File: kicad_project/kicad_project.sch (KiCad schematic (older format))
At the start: 157 parts, among them U1 SST39SF010, U11 AS6C4008-55PCN, U12 74LS85, U13 74LS85, U14 74LS283, U15 AS6C4008-55PCN, U16 74HC245, U17 74HC245, U18 74LS283, U19 74HC86, U2 SST39SF010, U20 74HC245, U21 74HC245, U22 74HC245, U23 SST39SF010, U24 74HC86, U25 74LS283, U26 74HC245, U27 74HC245, U28 74HC245, U29 74HC86, U3 74HC245, U30 74LS283, U31 SST39SF010, U4 74HC245, U5 74LS161, U6 74HC245, U7 74HC245, U8 74HC245, U9 SST39SF010

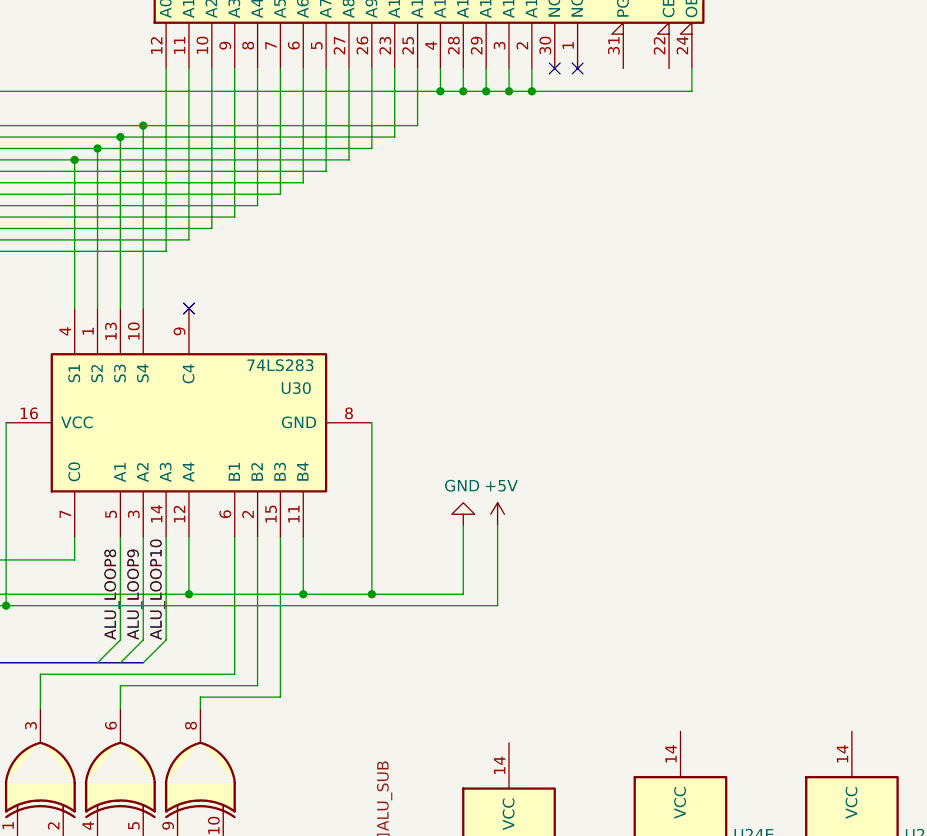
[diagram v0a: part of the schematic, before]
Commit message: Added some flashing tools, and misc...
Signed-off-by: Dave Butler <croepha@gmail.com>
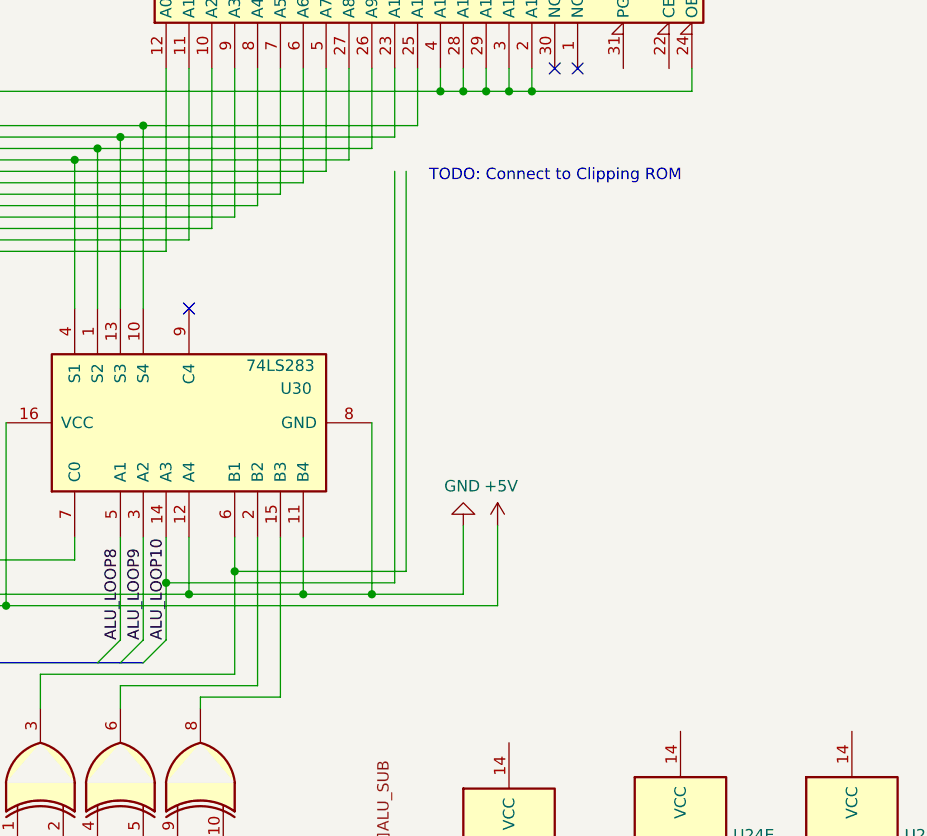
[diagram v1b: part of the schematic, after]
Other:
- note added: "TODO: Connect to Clipping ROM"

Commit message: .
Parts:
- added R?: 10K, symbol Device:R
- added U? (x6): 74HC595, symbol 74xx:74HC595
- added U? (x2): 74AHC04, symbol 74xx:74AHC04
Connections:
- net labels added: PRGM#, PRGMCLK, PRGMIN, PRGMOUT
- wire segments 1643 -> 1888
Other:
- moved on the sheet: R1, R2, R3, R4, U11, U12, U13, U14, U15, U16, U17, U5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

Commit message: .
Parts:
- renumbered U9 to CONTROL2
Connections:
- net labels added: BUS_SIGN, PC_LDBUS#, PC_LDEND#, PC_LDSUM#, PC_SUM_SIGN
- net labels removed: PC_LD, PC_LDBUS, PC_LDEND, PC_LDSUM, PC_RNEG, PC_ROVR
- wire segments 1888 -> 1892
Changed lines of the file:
@@
 Connection ~ 4700 14750
 Wire Wire Line
-	5400 14750 7100 14750
+	5400 14750 6150 14750
 Connection ~ 5000 14750
 Wire Wire Line
 	5100 14750 5000 14750
 Wire Wire Line
-	4000 14750 4300 14750
+	4000 14750 4250 14750
 Wire Wire Line
 	4600 14750 4700 14750
@@
 	21100 8250 21100 8000
 Wire Wire Line
-	21100 8250 18150 8250
-Wire Wire Line
 	21000 8350 18150 8350
 Wire Wire Line
@@
 Wire Wire Line
 	16200 13850 16200 16500
-Wire Wire Line
-	16150 14050 16150 16400
 $Comp
 L Memory_RAM:AS6C4008-55PCN U15
@@
 	16200 16500 15700 16500
 Text HLabel 15700 16500 0    50   Output ~ 0
-PC_RNEG
-Text HLabel 15700 16400 0    50   Output ~ 0
-PC_ROVR
+PC_SUM_SIGN
+Text HLabel 17700 8250 0    50   Output ~ 0
+BUS_SIGN
 Wire Wire Line
 	17350 14350 17250 14350
@@
 PC_CEQE
 Text HLabel 14850 17050 2    50   Input ~ 0
-PC_LDEND
+PC_LDEND#
 Text HLabel 14850 16850 2    50   Input ~ 0
-PC_LDBUS
+PC_LDBUS#
 Text HLabel 14850 16950 2    50   Input ~ 0
-PC_LDSUM
+PC_LDSUM#
 Wire Wire Line
 	14850 16650 14750 16650
@@
 	25900 6200 25900 8400
 Wire Wire Line
-	15700 16400 16150 16400
-Wire Wire Line
 	19100 19000 19100 19750
 Wire Wire Line
@@
 Wire Wire Line
 	28150 3900 28150 3550
-Text HLabel 17250 3150 2    50   Output ~ 0
+Text HLabel 17250 3300 2    50   Output ~ 0
 WRITE_READY
-Text HLabel 15500 3300 3    50   Input ~ 0
+Text HLabel 15500 3950 3    50   Input ~ 0
 READY_DOWN
-Text HLabel 15400 3300 3    50   Input ~ 0
+Text HLabel 15400 3950 3    50   Input ~ 0
 READY_UP
-Text HLabel 15300 3300 3    50   Input ~ 0
+Text HLabel 15300 3950 3    50   Input ~ 0
 READY_RIGHT
-Text HLabel 15200 3300 3    50   Input ~ 0
+Text HLabel 15200 3950 3    50   Input ~ 0
 READY_LEFT
-Text HLabel 11250 3300 3    50   Input ~ 0
-ACC_NEG
-Text HLabel 11150 3300 3    50   Input ~ 0
-ACC_EQZ
-Text HLabel 11050 3300 3    50   Input ~ 0
-PC_ROVR
-Text HLabel 10950 3300 3    50   Input ~ 0
-PC_ROVR
-Text HLabel 10850 3300 3    50   Input ~ 0
-PC_ROVR
-Text HLabel 10750 3300 3    50   Input ~ 0
-PC_ROVR
 Wire Wire Line
 	18700 6700 18700 2850
@@
 NoConn ~ 17250 2750
 Wire Wire Line
-	20200 3050 20200 2850
+	20200 3200 20200 2850
 Wire Wire Line
 	20100 2950 20100 2850
 Wire Wire Line
-	20000 2850 20000 2950
-Connection ~ 20000 2950
-Wire Wire Line
-	20000 2950 20100 2950
-Wire Wire Line
-	19900 2850 19900 2950
-Connection ~ 19900 2950
-Wire Wire Line
-	19900 2950 20000 2950
-Wire Wire Line
-	19800 2850 19800 2950
-Connection ~ 19800 2950
-Wire Wire Line
-	19800 2950 19900 2950
-Wire Wire Line
-	19700 2850 19700 2950
-Connection ~ 19700 2950
-Wire Wire Line
-	19700 2950 19800 2950
-Wire Wire Line
-	19500 2950 19500 2850
-Connection ~ 19500 2950
-Wire Wire Line
-	19500 2950 19600 2950
-Wire Wire Line
-	19400 2850 19400 2950
-Connection ~ 19400 2950
-Wire Wire Line
-	19400 2950 19500 2950
-Wire Wire Line
-	19600 2850 19600 2950
-Connection ~ 19600 2950
-Wire Wire Line
-	19600 2950 19700 2950
-Wire Wire Line
 	9750 2850 9750 6700
 Wire Wire Line
-	16950 3050 20200 3050
+	16950 3200 20200 3200
 Connection ~ 15600 2950
 Wire Wire Line
@@
 Wire Wire Line
 	13900 2950 15600 2950
-Connection ~ 16950 3050
+Connection ~ 16950 3200
 Connection ~ 12500 3100
 Wire Wire Line
@@
 	12500 3100 15000 3100
 Wire Wire Line
-	15500 3300 15500 2850
+	15500 3950 15500 2850
 Wire Wire Line
-	15400 2850 15400 3300
+	15400 2850 15400 3950
 Wire Wire Line
-	15300 3300 15300 2850
+	15300 3950 15300 2850
 Wire Wire Line
-	15200 2850 15200 3300
+	15200 2850 15200 3950
 Wire Wire Line
-	15700 3050 16950 3050
+	15700 3200 16950 3200
 Wire Wire Line
-	15700 2850 15700 3050
+	15700 2850 15700 3200
 Wire Wire Line
-	16950 3050 16950 2750
+	16950 3200 16950 2750
 NoConn ~ 12700 2750
 Wire Wire Line
-	11250 2850 11250 3300
-Wire Wire Line
-	11150 3300 11150 2850
-Wire Wire Line
-	11050 2850 11050 3300
-Wire Wire Line
-	10950 3300 10950 2850
-Wire Wire Line
-	10850 2850 10850 3300
-Wire Wire Line
-	10750 3300 10750 2850
-Wire Wire Line
 	15100 3150 15100 2850
 Wire Wire Line
@@
 Wire Wire Line
 	9650 6750 9650 2850
-Connection ~ 18450 2950
 Wire Wire Line
 	15600 2950 18450 2950
 Wire Wire Line
-	18450 2950 19400 2950
-Wire Wire Line
 	18600 6750 18600 2850
 $Comp
@@
 	0    -1   1    0
 $EndComp
-Text HLabel 9650 1050 1    50   Output ~ 0
-PC_LD
-Text HLabel 9750 1050 1    50   Output ~ 0
-PC_LDEND
-Text HLabel 9850 1050 1    50   Output ~ 0
-PC_LDBUS
-Text HLabel 9950 1050 1    50   Output ~ 0
-PC_LDSUM
+Text HLabel 19000 1050 1    50   Output ~ 0
+PC_LD#
+Text HLabel 19100 1050 1    50   Output ~ 0
+PC_LDEND#
+Text HLabel 19200 1050 1    50   Output ~ 0
+PC_LDBUS#
+Text HLabel 19300 1050 1    50   Output ~ 0
+PC_LDSUM#
 Wire Wire Line
-	9650 1050 9650 1650
+	19000 1050 19000 1650
 Wire Wire Line
-	9750 1650 9750 1050
+	19100 1650 19100 1050
 Wire Wire Line
-	9850 1050 9850 1650
+	19200 1050 19200 1650
 Wire Wire Line
-	9950 1050 9950 1650
+	19300 1050 19300 1650
 Text HLabel 10050 1050 1    50   Output ~ 0
 G_LEFT
@@
 H1
 Text HLabel 14300 1050 1    50   Output ~ 0
-H1
+H2
 NoConn ~ 12700 1750
 Wire Wire Line
@@
 Connection ~ 17950 1450
 Wire Wire Line
-	19100 1050 19100 1650
-Text HLabel 19100 1050 1    50   Output ~ 0
+	9750 1050 9750 1650
+Text HLabel 9750 1050 1    50   Output ~ 0
 ALU_RDACC#
 Wire Wire Line
@@
 	18600 1050 18600 1650
 Wire Wire Line
-	19300 1650 19300 1050
+	9950 1650 9950 1050
 Wire Wire Line
-	19200 1050 19200 1650
-Text HLabel 19300 1050 1    50   Output ~ 0
+	9850 1050 9850 1650
+Text HLabel 9950 1050 1    50   Output ~ 0
 BAK_RESTORE#
-Text HLabel 19200 1050 1    50   Output ~ 0
+Text HLabel 9850 1050 1    50   Output ~ 0
 BAK_SAVE#
 Wire Wire Line
-	19000 1050 19000 1650
-Text HLabel 19000 1050 1    50   Output ~ 0
+	9650 1050 9650 1650
+Text HLabel 9650 1050 1    50   Output ~ 0
 ALU_WRACC#
 Text HLabel 18800 1050 1    50   Output ~ 0
@@
 NoConn ~ 17050 1750
 $Comp
-L Memory_Flash:SST39SF010 U9
+L Memory_Flash:SST39SF010 CONTROL2
 U 1 1 9D597AA5
 P 19800 2250
-F 0 "U9" V 20100 2050 50  0000 C CNN
+F 0 "CONTROL2" V 20100 1350 50  0000 C CNN
 F 1 "SST39SF010" V 20100 2400 50  0000 C CNN
 F 2 "" H 19800 2550 50  0001 C CNN
@@
 	16100 8100 16750 8100
 Wire Wire Line
-	16950 3050 16950 3150
+	16950 3200 16950 3300
 Wire Wire Line
-	16950 3150 17250 3150
+	16950 3300 17250 3300
 Connection ~ 16150 8150
 Wire Wire Line
@@
 TODO: Connect to Clipping ROM
 Wire Wire Line
-	5600 5000 6900 5000
-Wire Bus Line
-	6800 3650 6800 6000
-Wire Wire Line
 	16100 6900 16100 7500
 Connection ~ 16100 7500
@@
 Connection ~ 16950 6050
 Connection ~ 17050 6000
-Wire Wire Line
-	11950 3000 9550 3000
 Connection ~ 11950 3000
 Wire Wire Line
@@
 Wire Wire Line
 	12200 8800 12200 8600
-Wire Wire Line
-	11700 8800 11800 8800
 Connection ~ 11700 8800
 Wire Wire Line
@@
 Wire Wire Line
 	12200 8900 11800 8900
-Wire Wire Line
-	11800 8900 11800 8800
-Connection ~ 11800 8800
-Wire Wire Line
-	11800 8800 11900 8800
 Connection ~ 12200 8600
 Wire Wire Line
@@
 	12250 6750 12250 11400
 Wire Wire Line
+	5600 5000 6900 5000
+Wire Bus Line
+	6800 3650 6800 6000
+Wire Wire Line
+	6150 14750 6150 15450
+Connection ~ 6150 14750
+Wire Wire Line
+	6150 14750 7100 14750
+Wire Wire Line
+	4250 14750 4250 14900
+Wire Wire Line
+	4250 14900 6050 14900
+Wire Wire Line
+	6050 14900 6050 15450
+Connection ~ 4250 14750
+Wire Wire Line
+	4250 14750 4300 14750
+Wire Wire Line
+	19400 3650 19400 2850
+Wire Wire Line
+	19500 2850 19500 3650
+Wire Wire Line
+	19600 3650 19600 2850
+Wire Wire Line
+	19700 2850 19700 3650
+Wire Wire Line
+	19800 3650 19800 2850
+Wire Wire Line
+	19900 2850 19900 3650
+Text HLabel 19400 3650 3    50   Input ~ 0
+PC_SUM_SIGN
+Text HLabel 19500 3650 3    50   Input ~ 0
+BUS_SIGN
+Text HLabel 19600 3650 3    50   Input ~ 0
+PC_SGTE
+Text HLabel 19700 3650 3    50   Input ~ 0
+PC_CEQE
+Text HLabel 19800 3650 3    50   Input ~ 0
+ACC_EQZ
+Text HLabel 19900 3650 3    50   Input ~ 0
+ACC_NEG
+Wire Wire Line
+	18450 2950 20000 2950
+Connection ~ 18450 2950
+Wire Wire Line
+	20000 2850 20000 2950
+Connection ~ 20000 2950
+Wire Wire Line
+	20000 2950 20100 2950
+Wire Wire Line
+	15700 3200 10750 3200
+Wire Wire Line
+	10750 3200 10750 2850
+Connection ~ 15700 3200
+Wire Wire Line
+	13900 2950 11250 2950
+Wire Wire Line
+	10850 2950 10850 2850
+Connection ~ 13900 2950
+Wire Wire Line
+	10950 2850 10950 2950
+Connection ~ 10950 2950
+Wire Wire Line
+	10950 2950 10850 2950
+Connection ~ 11050 2950
+Wire Wire Line
+	11050 2950 10950 2950
+Wire Wire Line
+	11050 2850 11050 2950
+Wire Wire Line
+	11150 2850 11150 2950
+Connection ~ 11150 2950
+Wire Wire Line
+	11150 2950 11050 2950
+Wire Wire Line
+	11950 3000 9550 3000
+Wire Wire Line
+	11250 2850 11250 2950
+Connection ~ 11250 2950
+Wire Wire Line
+	11250 2950 11150 2950
+Wire Wire Line
+	11700 8800 11900 8800
+Wire Wire Line
+	11800 8900 11800 8850
+Wire Wire Line
+	11800 8850 11300 8850
+Wire Wire Line
 	5500 5100 6900 5100
 Wire Wire Line
@@
 Wire Wire Line
 	4500 6100 6900 6100
+Wire Wire Line
+	17700 8250 21100 8250
 Wire Bus Line
 	6300 4300 6700 4300
